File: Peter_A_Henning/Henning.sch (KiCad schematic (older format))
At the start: 19 parts, among them P1 RS232, P2 EBUS, Q1 BD645, U1 4011, U2 CNY17-1, U3 78L05, U4 CNY17-1

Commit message: Re-generated Henning's board using a different terminal block.
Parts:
- P2: footprint Terminal_Blocks:TerminalBlock_WAGO-236_2Stift_RM5mm_2pol -> Terminal_Blocks:TerminalBlock_Pheonix_MPT-2.54mm_2pol
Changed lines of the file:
@@
 F 0 "P2" H 9200 5400 50  0000 C CNN
 F 1 "EBUS" V 9300 5250 50  0000 C CNN
-F 2 "Terminal_Blocks:TerminalBlock_WAGO-236_2Stift_RM5mm_2pol" H 9200 5250 50  0001 C CNN
+F 2 "Terminal_Blocks:TerminalBlock_Pheonix_MPT-2.54mm_2pol" H 9200 5250 50  0001 C CNN
 F 3 "" H 9200 5250 50  0000 C CNN
 	1    9200 5250

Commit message: Ditto for Henning's design.
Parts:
- P2: footprint Terminal_Blocks:TerminalBlock_Pheonix_MPT-2.54mm_2pol -> Terminal_Blocks:TerminalBlock_Pheonix_MKDS1.5-2pol
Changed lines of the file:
@@
 F 0 "P2" H 9200 5400 50  0000 C CNN
 F 1 "EBUS" V 9300 5250 50  0000 C CNN
-F 2 "Terminal_Blocks:TerminalBlock_Pheonix_MPT-2.54mm_2pol" H 9200 5250 50  0001 C CNN
+F 2 "Terminal_Blocks:TerminalBlock_Pheonix_MKDS1.5-2pol" H 9200 5250 50  0001 C CNN
 F 3 "" H 9200 5250 50  0000 C CNN
 	1    9200 5250

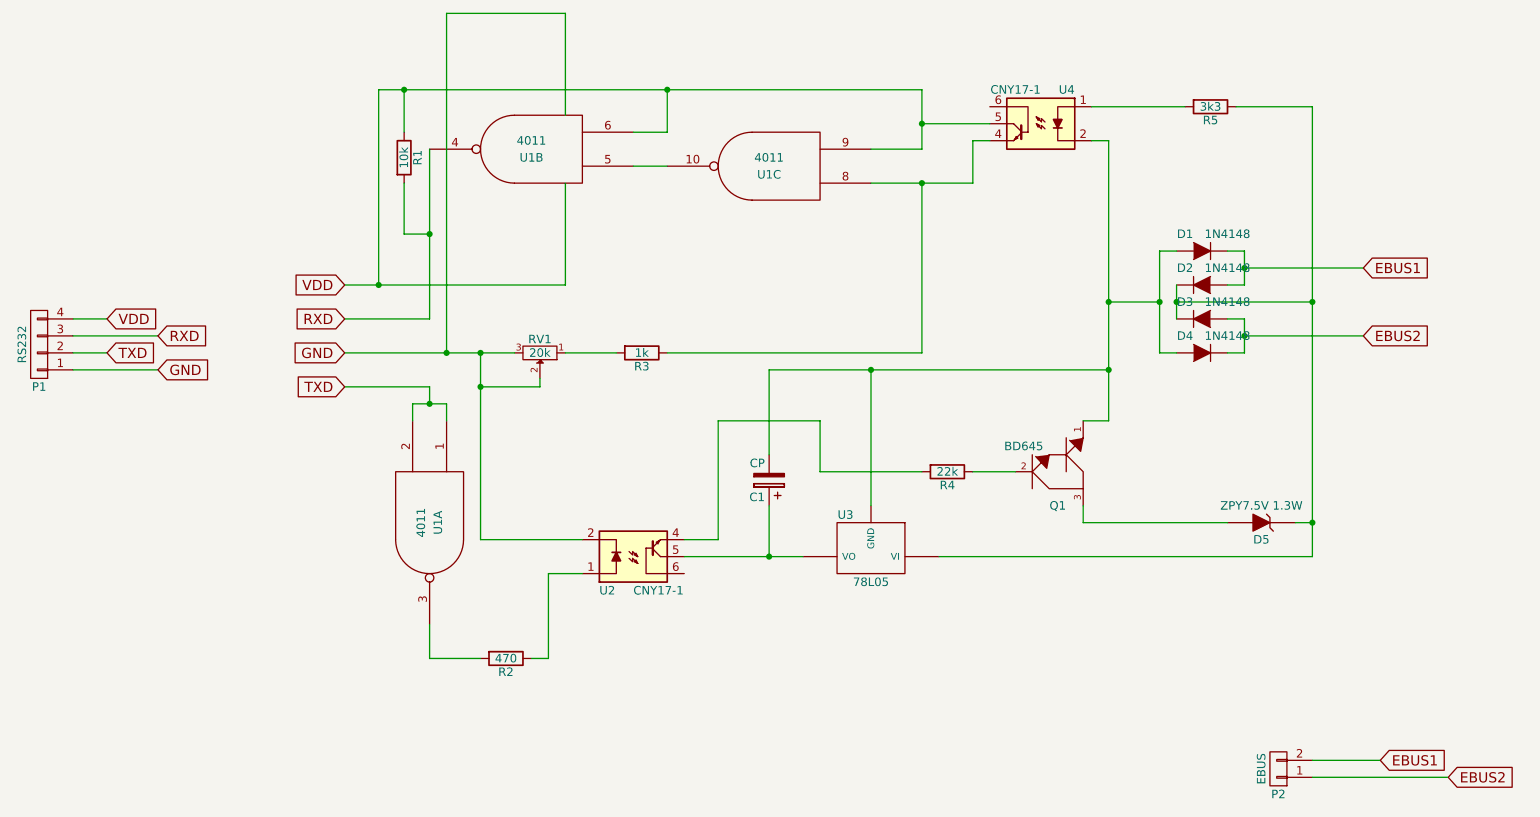
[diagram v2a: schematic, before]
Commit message: Fixed a silly error - reversed some polarities, no wonder this whole thing didn't work.
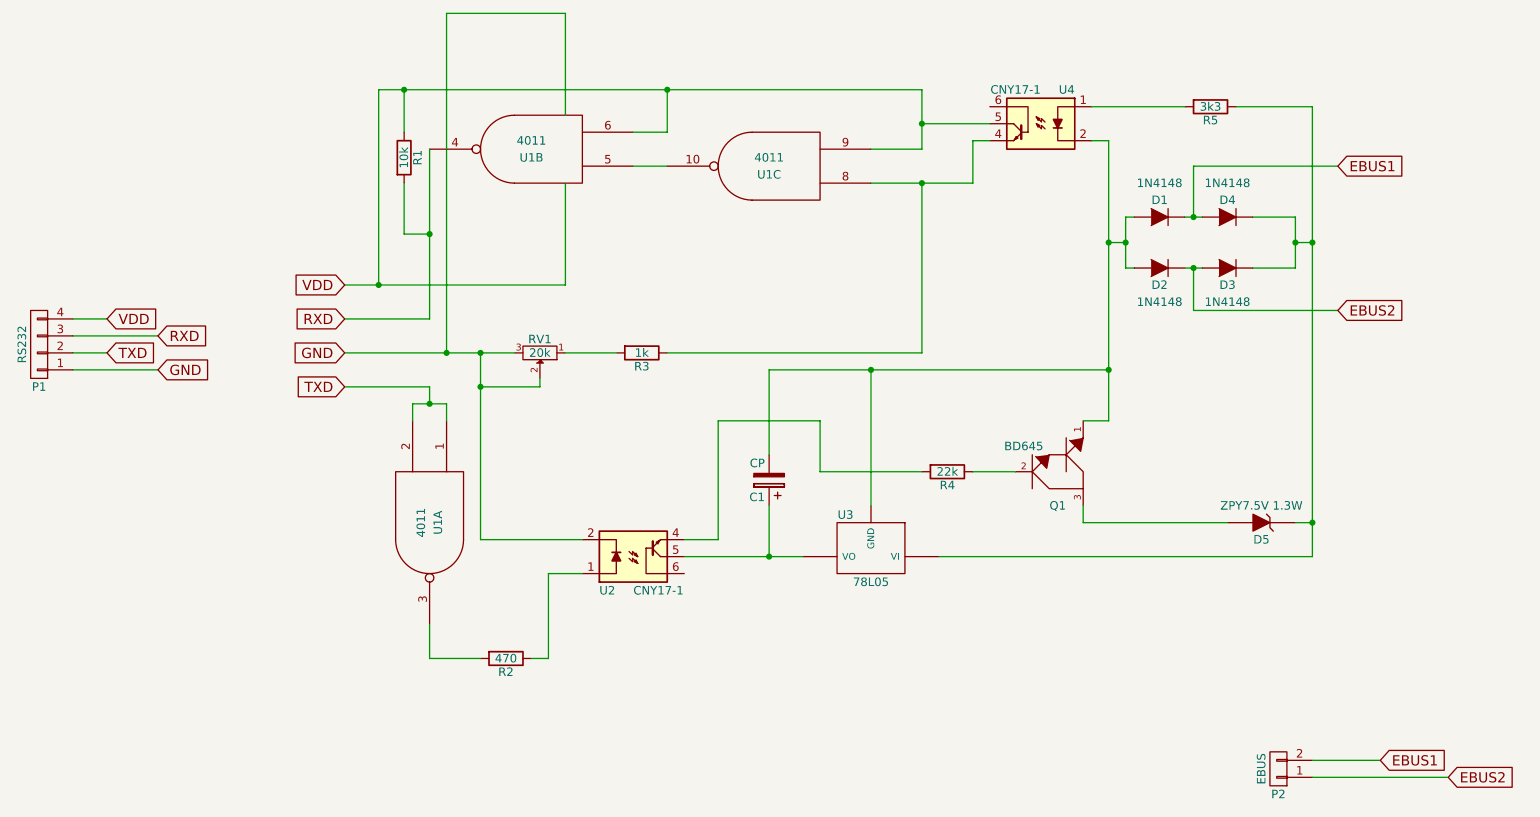
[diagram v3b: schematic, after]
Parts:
- U3: footprint TO_SOT_Packages_THT:TO-92_Molded_Wide -> TO_SOT_Packages_THT:TO-220_Neutral123_Horizontal
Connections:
- net EBUS1: now also D4.2 (A); no longer D2.2 (A)
- net EBUS2: now also D2.1 (K); no longer D4.1 (K)
- net at D3.1 (K), D5.1 (K), R5.1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: now also D4.1 (K); no longer D2.1 (K)
- net at C1.2, D1.2 (A), Q1.1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: now also D2.2 (A); no longer D4.2 (A)
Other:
- moved on the sheet: D1, D2, D3, D4
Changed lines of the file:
@@
 Comment4 ""
 $EndDescr
-Text GLabel 9700 2300 2    60   Input ~ 0
+Text GLabel 9550 1700 2    60   Input ~ 0
 EBUS1
-Text GLabel 9700 2700 2    60   Input ~ 0
+Text GLabel 9550 2550 2    60   Input ~ 0
 EBUS2
 $Comp
@@
 F 0 "U3" H 6950 3754 50  0000 C CNN
 F 1 "78L05" H 6800 4150 50  0000 C CNN
-F 2 "TO_SOT_Packages_THT:TO-92_Molded_Wide" H 6800 3950 50  0001 C CNN
+F 2 "TO_SOT_Packages_THT:TO-220_Neutral123_Horizontal" H 6800 3950 50  0001 C CNN
 F 3 "" H 6800 3950 50  0000 C CNN
 	1    6800 3950
@@
 	4050 2100 4200 2100
 Wire Wire Line
-	4200 2600 4200 1600
-Wire Wire Line
-	3700 2600 4200 2600
+	4200 1600 4200 2600
+Wire Wire Line
+	4200 2600 3700 2600
 Connection ~ 4200 2100
 $Comp
@@
 Connection ~ 4500 3000
 Wire Wire Line
-	5100 3900 4500 3900
-Wire Wire Line
-	4500 3900 4500 2800
+	4500 3900 5100 3900
+Wire Wire Line
+	4500 2800 4500 3900
 Wire Wire Line
 	4900 4100 5100 4100
@@
 L D D1
 U 1 1 57E456DB
-P 8750 2200
-F 0 "D1" H 8850 2300 50  0000 C CNN
-F 1 "1N4148" H 8600 2300 50  0000 C CNN
-F 2 "Diodes_ThroughHole:Diode_DO-35_SOD27_Horizontal_RM10" H 8750 2200 50  0001 C CNN
-F 3 "" H 8750 2200 50  0000 C CNN
-	1    8750 2200
+P 8500 2000
+F 0 "D1" H 8500 2100 50  0000 C CNN
+F 1 "1N4148" H 8500 2200 50  0000 C CNN
+F 2 "Diodes_ThroughHole:Diode_DO-35_SOD27_Horizontal_RM10" H 8500 2000 50  0001 C CNN
+F 3 "" H 8500 2000 50  0000 C CNN
+	1    8500 2000
 	-1   0    0    -1
 $EndComp
@@
 L D D2
 U 1 1 57E45729
-P 8750 2400
-F 0 "D2" H 8650 2300 50  0000 C CNN
-F 1 "1N4148" H 8900 2300 50  0000 C CNN
-F 2 "Diodes_ThroughHole:Diode_DO-35_SOD27_Horizontal_RM10" H 8750 2400 50  0001 C CNN
-F 3 "" H 8750 2400 50  0000 C CNN
-	1    8750 2400
-	1    0    0    1
+P 8500 2300
+F 0 "D2" H 8500 2200 50  0000 C CNN
+F 1 "1N4148" H 8500 2100 50  0000 C CNN
+F 2 "Diodes_ThroughHole:Diode_DO-35_SOD27_Horizontal_RM10" H 8500 2300 50  0001 C CNN
+F 3 "" H 8500 2300 50  0000 C CNN
+	1    8500 2300
+	-1   0    0    -1
 $EndComp
 $Comp
 L D D3
 U 1 1 57E45775
-P 8750 2600
-F 0 "D3" H 8650 2500 50  0000 C CNN
-F 1 "1N4148" H 8900 2500 50  0000 C CNN
-F 2 "Diodes_ThroughHole:Diode_DO-35_SOD27_Horizontal_RM10" H 8750 2600 50  0001 C CNN
-F 3 "" H 8750 2600 50  0000 C CNN
-	1    8750 2600
-	1    0    0    1
+P 8900 2300
+F 0 "D3" H 8900 2200 50  0000 C CNN
+F 1 "1N4148" H 8900 2100 50  0000 C CNN
+F 2 "Diodes_ThroughHole:Diode_DO-35_SOD27_Horizontal_RM10" H 8900 2300 50  0001 C CNN
+F 3 "" H 8900 2300 50  0000 C CNN
+	1    8900 2300
+	-1   0    0    -1
 $EndComp
 $Comp
 L D D4
 U 1 1 57E457DF
-P 8750 2800
-F 0 "D4" H 8850 2900 50  0000 C CNN
-F 1 "1N4148" H 8600 2900 50  0000 C CNN
-F 2 "Diodes_ThroughHole:Diode_DO-35_SOD27_Horizontal_RM10" H 8750 2800 50  0001 C CNN
-F 3 "" H 8750 2800 50  0000 C CNN
-	1    8750 2800
+P 8900 2000
+F 0 "D4" H 8900 2100 50  0000 C CNN
+F 1 "1N4148" H 8900 2200 50  0000 C CNN
+F 2 "Diodes_ThroughHole:Diode_DO-35_SOD27_Horizontal_RM10" H 8900 2000 50  0001 C CNN
+F 3 "" H 8900 2000 50  0000 C CNN
+	1    8900 2000
 	-1   0    0    -1
 $EndComp
-Wire Wire Line
-	8900 2200 9000 2200
-Wire Wire Line
-	9000 2200 9000 2400
-Wire Wire Line
-	9000 2400 8900 2400
-Wire Wire Line
-	8900 2600 9000 2600
-Wire Wire Line
-	9000 2600 9000 2800
-Wire Wire Line
-	9000 2800 8900 2800
-Wire Wire Line
-	9700 2300 9000 2300
-Connection ~ 9000 2300
-Wire Wire Line
-	8600 2200 8500 2200
-Wire Wire Line
-	8500 2200 8500 2800
-Wire Wire Line
-	8500 2800 8600 2800
-Wire Wire Line
-	8600 2400 8600 2600
-Wire Wire Line
-	9400 2500 8600 2500
-Connection ~ 8600 2500
-Connection ~ 9400 2500
-Wire Wire Line
-	8500 2500 8200 2500
-Connection ~ 8200 2500
-Connection ~ 8500 2500
-Wire Wire Line
-	9000 2700 9700 2700
-Connection ~ 9000 2700
 $Comp
 L CONN_01X02 P2
@@
 	5000 2400 5000 1800
 Connection ~ 3900 2400
+Wire Wire Line
+	9050 2000 9300 2000
+Wire Wire Line
+	9050 2300 9300 2300
+Wire Wire Line
+	8650 2300 8750 2300
+Wire Wire Line
+	8650 2000 8750 2000
+Wire Wire Line
+	8350 2000 8300 2000
+Wire Wire Line
+	8300 2300 8350 2300
+Wire Wire Line
+	8300 2000 8300 2300
+Wire Wire Line
+	8300 2150 8200 2150
+Connection ~ 8200 2150
+Connection ~ 8300 2150
+Wire Wire Line
+	9300 2300 9300 2000
+Wire Wire Line
+	9300 2150 9400 2150
+Connection ~ 9400 2150
+Connection ~ 9300 2150
+Wire Wire Line
+	9550 1700 8700 1700
+Wire Wire Line
+	8700 1700 8700 2000
+Connection ~ 8700 2000
+Wire Wire Line
+	8700 2300 8700 2550
+Wire Wire Line
+	8700 2550 9550 2550
+Connection ~ 8700 2300
 $EndSCHEMATC

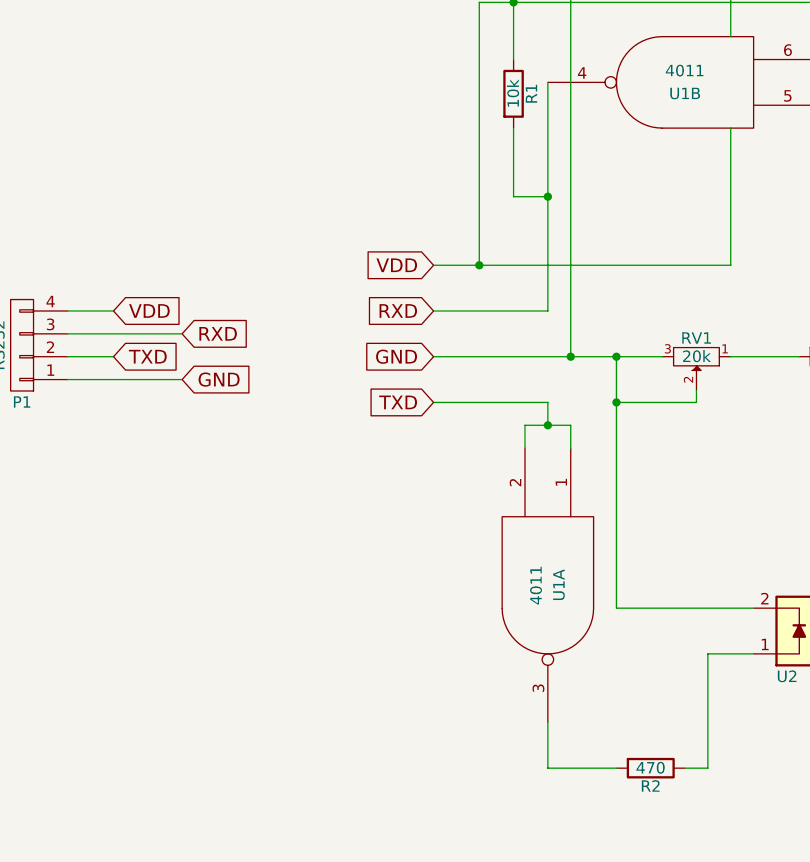
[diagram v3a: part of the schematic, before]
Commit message: Added a LED, regenerated production files.
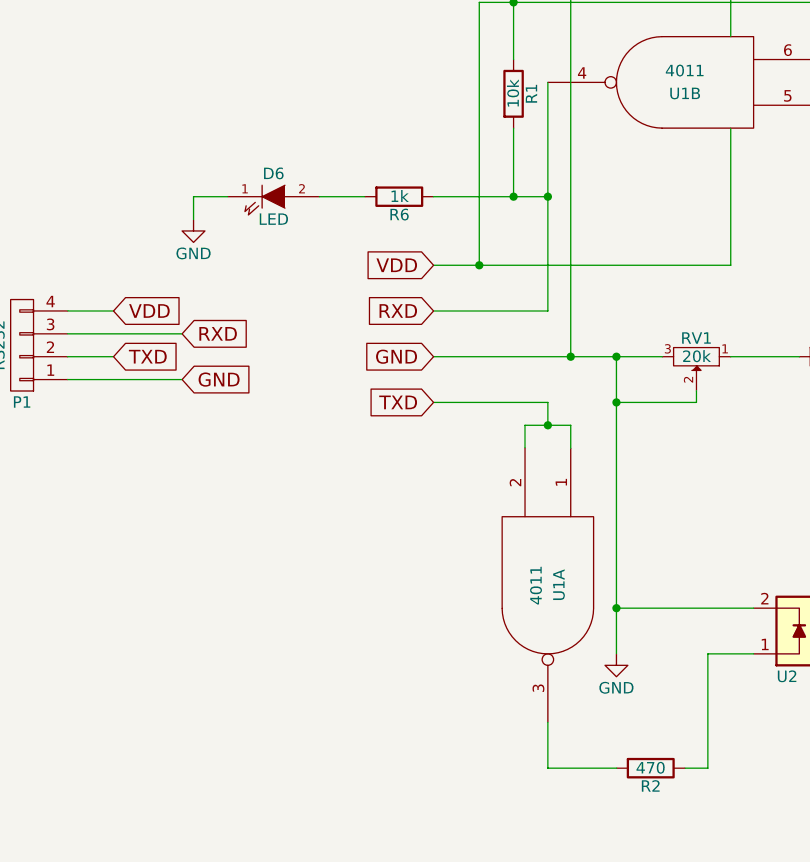
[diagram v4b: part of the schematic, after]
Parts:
- added D6: LED, LEDs:LED-5MM, symbol LED
- added R6: 1k, Resistors_ThroughHole:Resistor_Horizontal_RM10mm, symbol R
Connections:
- net RXD: now also R6.1
- net VSS renamed GND
- net GND: now also D6.1 (K)
- new net: D6.2 (A), R6.2
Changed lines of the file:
@@
 	4050 1800 4050 2100
 Wire Wire Line
-	4050 2100 4200 2100
+	3700 2100 4200 2100
 Wire Wire Line
 	4200 1600 4200 2600
@@
 	4500 3900 5100 3900
 Wire Wire Line
-	4500 2800 4500 3900
+	4500 2800 4500 4100
 Wire Wire Line
 	4900 4100 5100 4100
@@
 	8700 2550 9550 2550
 Connection ~ 8700 2300
+$Comp
+L R R6
+U 1 1 57EECB77
+P 3550 2100
+F 0 "R6" V 3630 2100 50  0000 C CNN
+F 1 "1k" V 3550 2100 50  0000 C CNN
+F 2 "Resistors_ThroughHole:Resistor_Horizontal_RM10mm" V 3480 2100 50  0001 C CNN
+F 3 "" H 3550 2100 50  0000 C CNN
+	1    3550 2100
+	0    1    1    0
+$EndComp
+$Comp
+L LED D6
+U 1 1 57EECBCD
+P 3000 2100
+F 0 "D6" H 3000 2200 50  0000 C CNN
+F 1 "LED" H 3000 2000 50  0000 C CNN
+F 2 "LEDs:LED-5MM" H 3000 2100 50  0001 C CNN
+F 3 "" H 3000 2100 50  0000 C CNN
+	1    3000 2100
+	1    0    0    -1
+$EndComp
+$Comp
+L GND #PWR01
+U 1 1 57EECC9B
+P 2650 2200
+F 0 "#PWR01" H 2650 1950 50  0001 C CNN
+F 1 "GND" H 2650 2050 50  0000 C CNN
+F 2 "" H 2650 2200 50  0000 C CNN
+F 3 "" H 2650 2200 50  0000 C CNN
+	1    2650 2200
+	1    0    0    -1
+$EndComp
+$Comp
+L GND #PWR02
+U 1 1 57EECCF4
+P 4500 4100
+F 0 "#PWR02" H 4500 3850 50  0001 C CNN
+F 1 "GND" H 4500 3950 50  0000 C CNN
+F 2 "" H 4500 4100 50  0000 C CNN
+F 3 "" H 4500 4100 50  0000 C CNN
+	1    4500 4100
+	1    0    0    -1
+$EndComp
+Connection ~ 4500 3900
+Connection ~ 4050 2100
+Wire Wire Line
+	3400 2100 3200 2100
+Wire Wire Line
+	2800 2100 2650 2100
+Wire Wire Line
+	2650 2100 2650 2200
 $EndSCHEMATC
